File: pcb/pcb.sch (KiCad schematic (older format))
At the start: 23 parts, among them J1 Screw_Terminal_01x06, J10 Screw_Terminal_01x04, J2 pin header, J3 Screw_Terminal_01x07, J4 Screw_Terminal_01x02, J5 Screw_Terminal_01x04, J6 JST XH-2P, J7 JST XH-3P, J8 JST XH-4P, J9 Screw_Terminal_01x04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

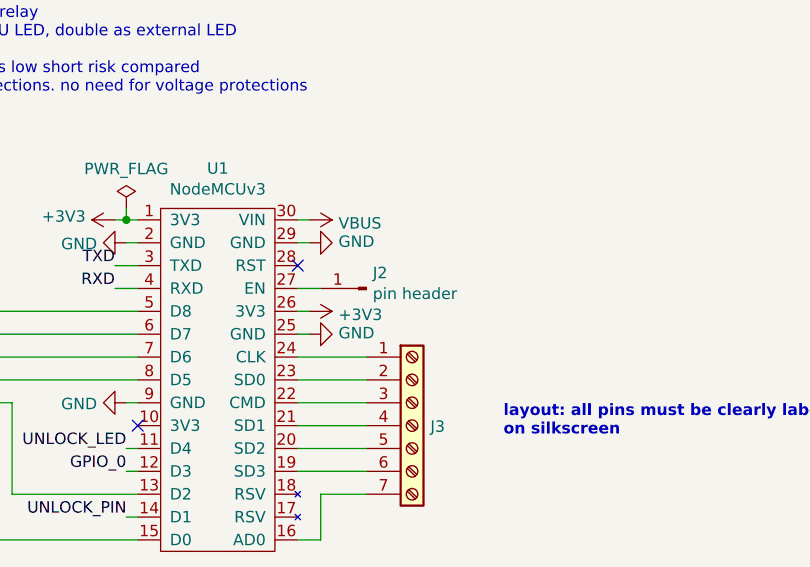
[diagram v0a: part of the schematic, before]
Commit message: all-but-zener footprint assignment
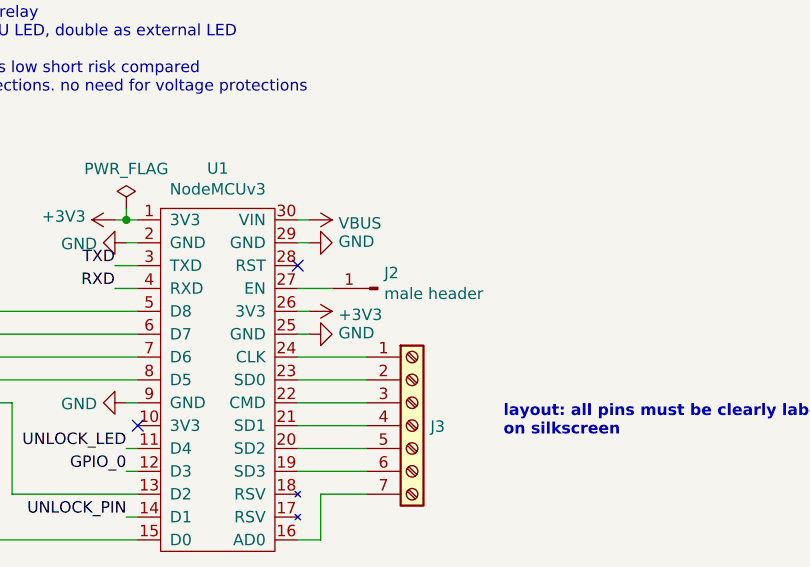
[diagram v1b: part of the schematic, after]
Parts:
- D1, D2, D3: footprint (none) -> LED_THT:LED_D5.0mm
- D5, D8: footprint Diode_THT:D_DO-41_SOD81_P10.16mm_Horizontal -> Diode_THT:D_P600_R-6_P7.62mm_Vertical_AnodeUp
- J1: footprint (none) -> TerminalBlock_Phoenix:TerminalBlock_Phoenix_MPT-0,5-6-2.54_1x06_P2.54mm_Horizontal
- J10, J5, J9: footprint (none) -> TerminalBlock_Phoenix:TerminalBlock_Phoenix_MPT-0,5-4-2.54_1x04_P2.54mm_Horizontal
- J2: value pin header -> male header; footprint (none) -> Connector_PinHeader_2.54mm:PinHeader_1x01_P2.54mm_Vertical
- J3: footprint (none) -> TerminalBlock_Phoenix:TerminalBlock_Phoenix_MPT-0,5-7-2.54_1x07_P2.54mm_Horizontal
- J4: footprint (none) -> TerminalBlock_Phoenix:TerminalBlock_Phoenix_MPT-0,5-2-2.54_1x02_P2.54mm_Horizontal
- J6: footprint (none) -> Connector_JST:JST_XH_B2B-XH-A_1x02_P2.50mm_Vertical
- J7: footprint (none) -> Connector_JST:JST_XH_B3B-XH-A_1x03_P2.50mm_Vertical
- J8: footprint (none) -> Connector_JST:JST_XH_B4B-XH-A_1x04_P2.50mm_Vertical
- R1, R2, R3: footprint (none) -> Resistor_THT:R_Axial_DIN0204_L3.6mm_D1.6mm_P2.54mm_Vertical
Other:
- moved on the sheet: J2
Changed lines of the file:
@@
 F 0 "J4" H 8230 2946 50  0000 L CNN
 F 1 "Screw_Terminal_01x02" H 8230 2901 50  0001 L CNN
-F 2 "" H 8150 3000 50  0001 C CNN
+F 2 "TerminalBlock_Phoenix:TerminalBlock_Phoenix_MPT-0,5-2-2.54_1x02_P2.54mm_Horizontal" H 8150 3000 50  0001 C CNN
 F 3 "~" H 8150 3000 50  0001 C CNN
 	1    8150 3000
@@
 F 0 "R2" H 6750 6050 50  0000 R CNN
 F 1 "1k" V 6800 6100 50  0000 R CNN
-F 2 "" H 6800 6050 50  0001 C CNN
+F 2 "Resistor_THT:R_Axial_DIN0204_L3.6mm_D1.6mm_P2.54mm_Vertical" H 6800 6050 50  0001 C CNN
 F 3 "~" H 6800 6050 50  0001 C CNN
 	1    6800 6050
@@
 F 0 "D2" V 6846 6232 50  0000 R CNN
 F 1 "GN" V 6755 6232 50  0000 R CNN
-F 2 "" V 6800 6300 50  0001 C CNN
+F 2 "LED_THT:LED_D5.0mm" V 6800 6300 50  0001 C CNN
 F 3 "~" V 6800 6300 50  0001 C CNN
 	1    6800 6300
@@
 F 0 "R1" H 6450 6050 50  0000 R CNN
 F 1 "1k" V 6500 6100 50  0000 R CNN
-F 2 "" H 6500 6050 50  0001 C CNN
+F 2 "Resistor_THT:R_Axial_DIN0204_L3.6mm_D1.6mm_P2.54mm_Vertical" H 6500 6050 50  0001 C CNN
 F 3 "~" H 6500 6050 50  0001 C CNN
 	1    6500 6050
@@
 F 0 "D1" V 6546 6232 50  0000 R CNN
 F 1 "GN" V 6455 6232 50  0000 R CNN
-F 2 "" V 6500 6300 50  0001 C CNN
+F 2 "LED_THT:LED_D5.0mm" V 6500 6300 50  0001 C CNN
 F 3 "~" V 6500 6300 50  0001 C CNN
 	1    6500 6300
@@
 F 0 "R3" H 7050 6050 50  0000 R CNN
 F 1 "1k" V 7100 6100 50  0000 R CNN
-F 2 "" H 7100 6050 50  0001 C CNN
+F 2 "Resistor_THT:R_Axial_DIN0204_L3.6mm_D1.6mm_P2.54mm_Vertical" H 7100 6050 50  0001 C CNN
 F 3 "~" H 7100 6050 50  0001 C CNN
 	1    7100 6050
@@
 F 0 "D3" V 7146 6232 50  0000 R CNN
 F 1 "RD" V 7055 6232 50  0000 R CNN
-F 2 "" V 7100 6300 50  0001 C CNN
+F 2 "LED_THT:LED_D5.0mm" V 7100 6300 50  0001 C CNN
 F 3 "~" V 7100 6300 50  0001 C CNN
 	1    7100 6300
@@
 L Connector:Conn_01x01_Male J2
 U 1 1 629AF30A
-P 2850 6550
-F 0 "J2" H 2822 6482 50  0000 R CNN
-F 1 "pin header" H 2822 6573 50  0000 R CNN
-F 2 "" H 2850 6550 50  0001 C CNN
-F 3 "~" H 2850 6550 50  0001 C CNN
-	1    2850 6550
+P 2900 6550
+F 0 "J2" H 2872 6482 50  0000 R CNN
+F 1 "male header" H 2872 6573 50  0000 R CNN
+F 2 "Connector_PinHeader_2.54mm:PinHeader_1x01_P2.54mm_Vertical" H 2900 6550 50  0001 C CNN
+F 3 "~" H 2900 6550 50  0001 C CNN
+	1    2900 6550
 	-1   0    0    1
 $EndComp
-Wire Wire Line
-	2650 6550 2550 6550
 NoConn ~ 1850 7150
 Wire Wire Line
@@
 F 0 "J1" H 1050 6800 50  0000 C CNN
 F 1 "Screw_Terminal_01x06" H 1200 6900 50  0001 C CNN
-F 2 "" H 900 6950 50  0001 C CNN
+F 2 "TerminalBlock_Phoenix:TerminalBlock_Phoenix_MPT-0,5-6-2.54_1x06_P2.54mm_Horizontal" H 900 6950 50  0001 C CNN
 F 3 "~" H 900 6950 50  0001 C CNN
 	1    900  6950
@@
 F 0 "J3" H 3130 7146 50  0000 L CNN
 F 1 "Screw_Terminal_01x07" H 3130 7101 50  0001 L CNN
-F 2 "" H 3050 7150 50  0001 C CNN
+F 2 "TerminalBlock_Phoenix:TerminalBlock_Phoenix_MPT-0,5-7-2.54_1x07_P2.54mm_Horizontal" H 3050 7150 50  0001 C CNN
 F 3 "~" H 3050 7150 50  0001 C CNN
 	1    3050 7150
@@
 F 0 "D5" H 7400 3205 50  0000 C CNN
 F 1 "1N4004" H 7400 3114 50  0000 C CNN
-F 2 "Diode_THT:D_DO-41_SOD81_P10.16mm_Horizontal" H 7400 2825 50  0001 C CNN
+F 2 "Diode_THT:D_P600_R-6_P7.62mm_Vertical_AnodeUp" H 7400 2825 50  0001 C CNN
 F 3 "http://www.vishay.com/docs/88503/1n4001.pdf" H 7400 3000 50  0001 C CNN
 	1    7400 3000
@@
 F 0 "D8" V 10146 1332 50  0000 R CNN
 F 1 "1N4004" V 10055 1332 50  0000 R CNN
-F 2 "Diode_THT:D_DO-41_SOD81_P10.16mm_Horizontal" H 10100 1225 50  0001 C CNN
+F 2 "Diode_THT:D_P600_R-6_P7.62mm_Vertical_AnodeUp" H 10100 1225 50  0001 C CNN
 F 3 "http://www.vishay.com/docs/88503/1n4001.pdf" H 10100 1400 50  0001 C CNN
 	1    10100 1400
@@
 F 0 "J10" H 9850 1400 50  0000 C CNN
 F 1 "Screw_Terminal_01x04" H 9850 1500 50  0001 C CNN
-F 2 "" H 9850 1800 50  0001 C CNN
+F 2 "TerminalBlock_Phoenix:TerminalBlock_Phoenix_MPT-0,5-4-2.54_1x04_P2.54mm_Horizontal" H 9850 1800 50  0001 C CNN
 F 3 "~" H 9850 1800 50  0001 C CNN
 	1    9850 1800
@@
 F 0 "J9" H 9350 1400 50  0000 C CNN
 F 1 "Screw_Terminal_01x04" H 9350 1500 50  0001 C CNN
-F 2 "" H 9350 1800 50  0001 C CNN
+F 2 "TerminalBlock_Phoenix:TerminalBlock_Phoenix_MPT-0,5-4-2.54_1x04_P2.54mm_Horizontal" H 9350 1800 50  0001 C CNN
 F 3 "~" H 9350 1800 50  0001 C CNN
 	1    9350 1800
@@
 F 0 "J5" H 8800 1400 50  0000 C CNN
 F 1 "Screw_Terminal_01x04" H 8800 1500 50  0001 C CNN
-F 2 "" H 8800 1800 50  0001 C CNN
+F 2 "TerminalBlock_Phoenix:TerminalBlock_Phoenix_MPT-0,5-4-2.54_1x04_P2.54mm_Horizontal" H 8800 1800 50  0001 C CNN
 F 3 "~" H 8800 1800 50  0001 C CNN
 	1    8800 1800
@@
 F 0 "J7" H 9208 5631 50  0000 C CNN
 F 1 "JST XH-3P" H 9208 5540 50  0000 C CNN
-F 2 "" H 9100 5350 50  0001 C CNN
+F 2 "Connector_JST:JST_XH_B3B-XH-A_1x03_P2.50mm_Vertical" H 9100 5350 50  0001 C CNN
 F 3 "https://www.amazon.com/GeeBat-460pcs-Connector-Housing-Adapter/dp/B01MCZE2HM/" H 9100 5350 50  0001 C CNN
 	1    9100 5350
@@
 F 0 "J6" H 9200 4650 50  0000 C CNN
 F 1 "JST XH-2P" H 9200 4550 50  0000 C CNN
-F 2 "" H 9100 4400 50  0001 C CNN
+F 2 "Connector_JST:JST_XH_B2B-XH-A_1x02_P2.50mm_Vertical" H 9100 4400 50  0001 C CNN
 F 3 "https://www.amazon.com/GeeBat-460pcs-Connector-Housing-Adapter/dp/B01MCZE2HM/" H 9100 4400 50  0001 C CNN
 	1    9100 4400
@@
 F 0 "J8" H 9208 6581 50  0000 C CNN
 F 1 "JST XH-4P" H 9208 6490 50  0000 C CNN
-F 2 "" H 9100 6300 50  0001 C CNN
+F 2 "Connector_JST:JST_XH_B4B-XH-A_1x04_P2.50mm_Vertical" H 9100 6300 50  0001 C CNN
 F 3 "https://www.amazon.com/GeeBat-460pcs-Connector-Housing-Adapter/dp/B01MCZE2HM/" H 9100 6300 50  0001 C CNN
 	1    9100 6300
@@
 	7850 3100 7900 3100
 Connection ~ 7900 3100
+Wire Wire Line
+	2550 6550 2700 6550
 $EndSCHEMATC

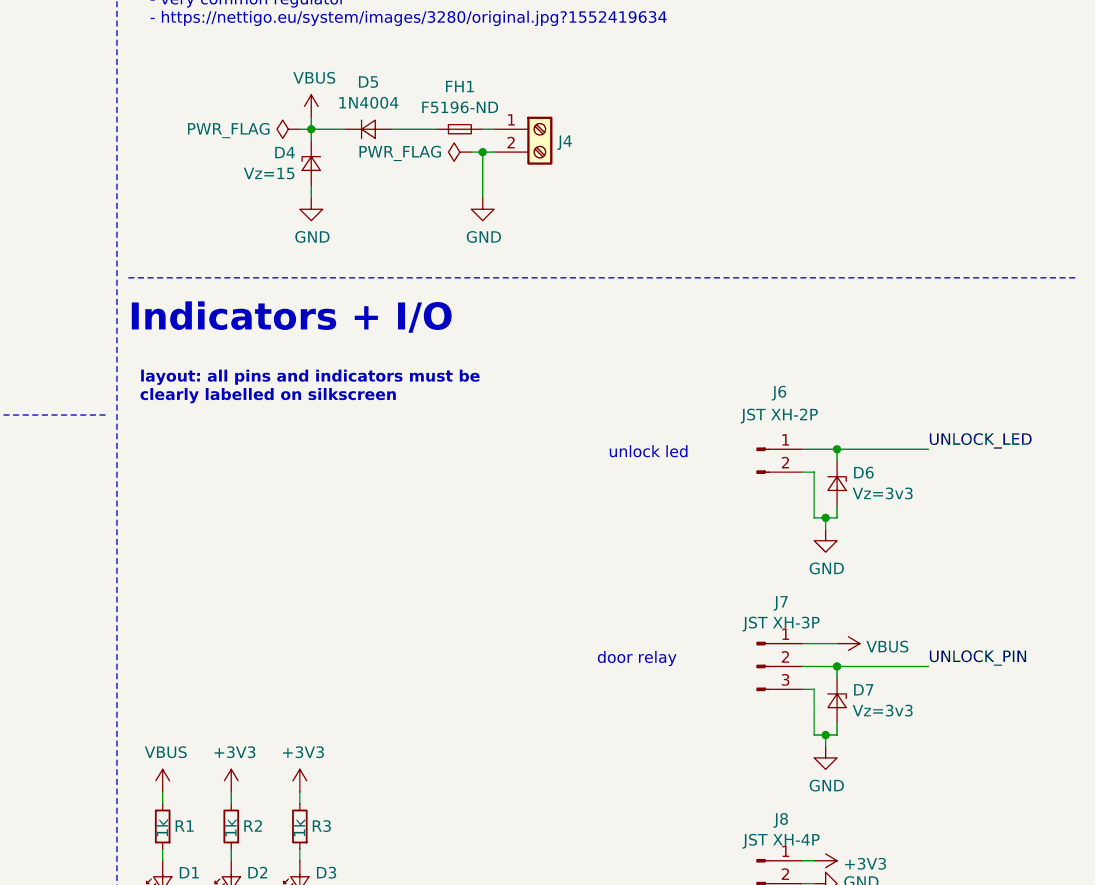
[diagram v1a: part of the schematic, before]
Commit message: zener selection + footprint assignment
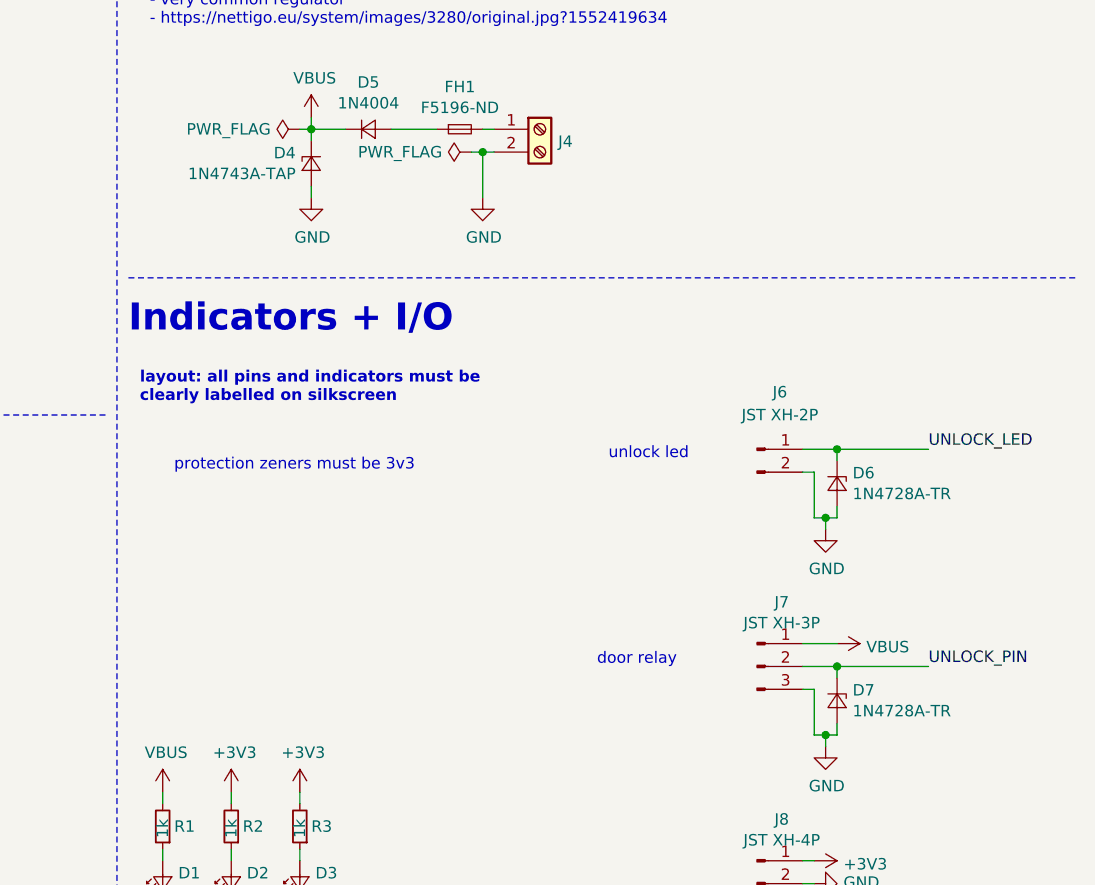
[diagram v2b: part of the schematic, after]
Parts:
- D4: value Vz=15 -> 1N4743A-TAP; footprint (none) -> Diode_THT:D_A-405_P2.54mm_Vertical_AnodeUp
- D6, D7: value Vz=3v3 -> 1N4728A-TR; footprint (none) -> Diode_THT:D_A-405_P2.54mm_Vertical_AnodeUp
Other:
- note added: "protection zeners must be 3v3"
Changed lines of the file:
@@
 P 7150 3150
 F 0 "D4" V 7104 3218 50  0000 L CNN
-F 1 "Vz=15" V 7195 3218 50  0000 L CNN
-F 2 "" V 7150 3150 50  0001 C CNN
-F 3 "~" V 7150 3150 50  0001 C CNN
+F 1 "1N4743A-TAP" V 7195 3218 50  0000 L CNN
+F 2 "Diode_THT:D_A-405_P2.54mm_Vertical_AnodeUp" V 7150 3150 50  0001 C CNN
+F 3 "https://www.digikey.com/en/products/detail/vishay-general-semiconductor-diodes-division/1N4743A-TAP/8564445?s=N4IgjCBcoLQBxVAYygMwIYBsDOBTANCAPZQDa4YATCALoC%2Bdh1k5YAcgCwDsHAzAIIwAKvwAKtOkA" V 7150 3150 50  0001 C CNN
 	1    7150 3150
 	0    -1   1    0
@@
 P 9450 5500
 F 0 "D7" V 9404 5568 50  0000 L CNN
-F 1 "Vz=3v3" V 9495 5568 50  0000 L CNN
-F 2 "" V 9450 5500 50  0001 C CNN
-F 3 "~" V 9450 5500 50  0001 C CNN
+F 1 "1N4728A-TR" V 9495 5568 50  0000 L CNN
+F 2 "Diode_THT:D_A-405_P2.54mm_Vertical_AnodeUp" V 9450 5500 50  0001 C CNN
+F 3 "https://www.digikey.com/en/products/detail/vishay-general-semiconductor-diodes-division/1N4728A-TR/3104058?s=N4IgjCBcoLQBxVAYygMwIYBsDOBTANCAPZQDa4YATCALoC%2Bdh1k5YAcgCwDslcAgjAAqAJVp0gA" V 9450 5500 50  0001 C CNN
 	1    9450 5500
 	0    1    1    0
@@
 P 9450 4550
 F 0 "D6" V 9404 4618 50  0000 L CNN
-F 1 "Vz=3v3" V 9495 4618 50  0000 L CNN
-F 2 "" V 9450 4550 50  0001 C CNN
+F 1 "1N4728A-TR" V 9495 4618 50  0000 L CNN
+F 2 "Diode_THT:D_A-405_P2.54mm_Vertical_AnodeUp" V 9450 4550 50  0001 C CNN
 F 3 "~" V 9450 4550 50  0001 C CNN
 	1    9450 4550
@@
 Wire Wire Line
 	2550 6550 2700 6550
+Text Notes 6550 4500 0    50   ~ 0
+protection zeners must be 3v3
 $EndSCHEMATC

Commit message: footprint rename: lolinv3->NodeMCUv3
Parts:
- U1: footprint project:lolinv3 -> project:NodeMCUv3
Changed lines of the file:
@@
 F 0 "U1" H 2200 6475 50  0000 C CNN
 F 1 "NodeMCUv3" H 2200 6384 50  0000 C CNN
-F 2 "project:lolinv3" H 2250 6350 50  0001 C CNN
+F 2 "project:NodeMCUv3" H 2250 6350 50  0001 C CNN
 F 3 "${KIPRJMOD}/../docs/NodeMCU-V3.pdf" H 2250 6350 50  0001 C CNN
 	1    1850 6250
